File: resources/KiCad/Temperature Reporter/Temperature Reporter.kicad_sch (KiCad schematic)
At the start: 9 parts, among them U1 ESP32-C3-0.42-OLED, U2 DS18B20, U3 DS18B20

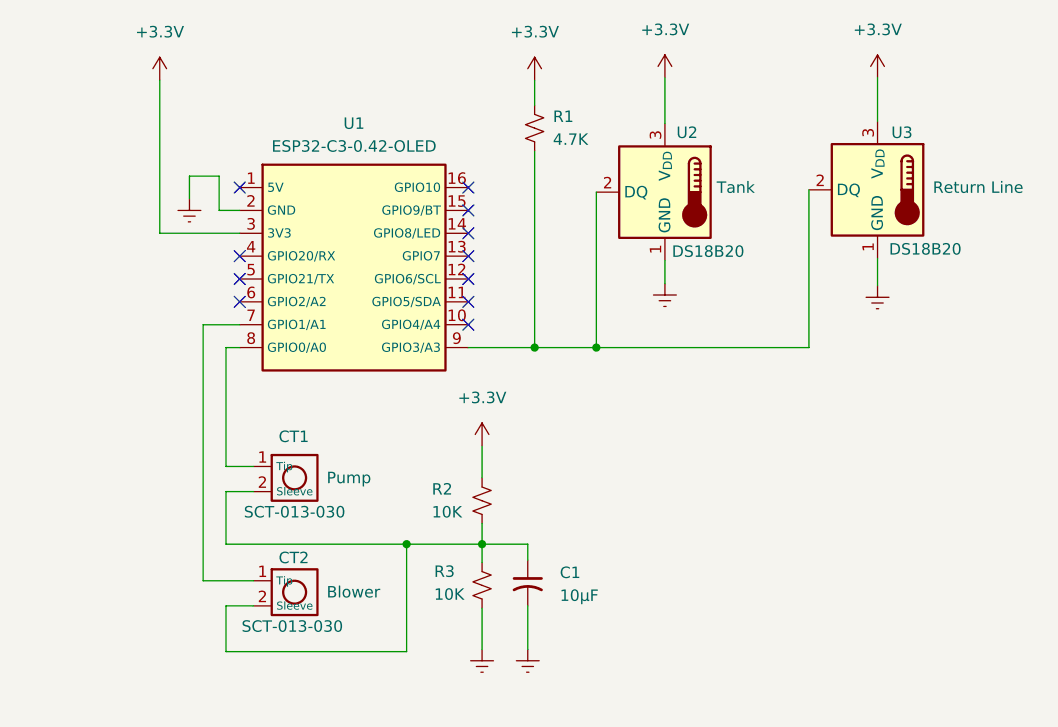
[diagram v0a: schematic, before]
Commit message: Added filter capacitors to the analog inputs
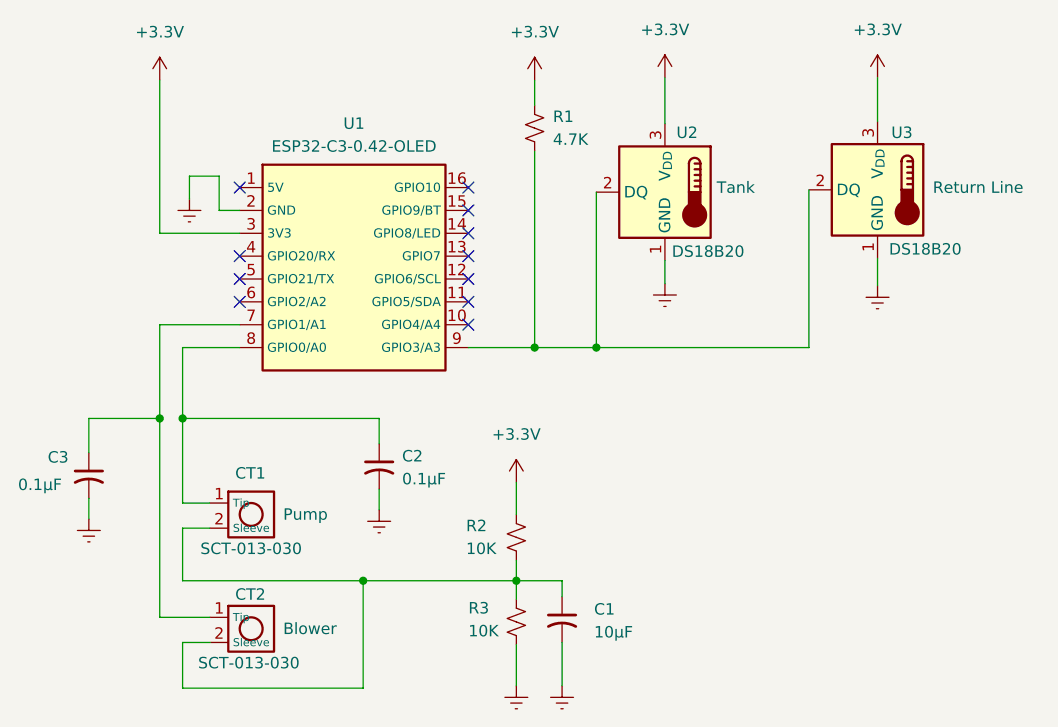
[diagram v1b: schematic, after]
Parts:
- added C2, C3: 0.1μF, symbol Device:C_Small_US
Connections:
- net Earth: now also C2.2, C3.2
- net at CT2.1 (Tip), U1.7 (GPIO1/A1): now also C3.1
- net at CT1.1 (Tip), U1.8 (GPIO0/A0): now also C2.1
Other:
- moved on the sheet: C1, CT1, CT2, R2, R3

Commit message: updated schematic
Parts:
- R2, R3: value 10K -> 1K
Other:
- moved on the sheet: C1, C2, C3, CT1, CT2, R2, R3, U1, U2, U3

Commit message: Changes to circuit board, board mount.  Added code to set the power to maximum.
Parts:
- C1, C2, C3: footprint (none) -> Capacitor_THT:C_Disc_D3.4mm_W2.1mm_P2.50mm
- CT1, CT2: footprint (none) -> Connector_PinHeader_2.54mm:PinHeader_1x02_P2.54mm_Horizontal
- R1, R2, R3: footprint (none) -> Resistor_THT:R_Axial_DIN0204_L3.6mm_D1.6mm_P2.54mm_Vertical
- U2, U3: footprint Package_TO_SOT_THT:TO-92_Inline -> Connector_PinHeader_2.54mm:PinHeader_1x03_P2.54mm_Horizontal
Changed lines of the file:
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@@
 			)
 		)
-		(property "Footprint" ""
+		(property "Footprint" "Capacitor_THT:C_Disc_D3.4mm_W2.1mm_P2.50mm"
 			(at 85.09 121.92 0)
 			(effects
@@
 			)
 		)
-		(property "Footprint" ""
+		(property "Footprint" "Connector_PinHeader_2.54mm:PinHeader_1x02_P2.54mm_Horizontal"
 			(at 103.632 138.43 0)
 			(effects
@@
 			)
 		)
-		(property "Footprint" "Package_TO_SOT_THT:TO-92_Inline"
+		(property "Footprint" "Connector_PinHeader_2.54mm:PinHeader_1x03_P2.54mm_Horizontal"
 			(at 198.12 96.52 0)
 			(effects
@@
 			)
 		)
-		(property "Footprint" ""
+		(property "Footprint" "Resistor_THT:R_Axial_DIN0204_L3.6mm_D1.6mm_P2.54mm_Vertical"
 			(at 132.08 128.27 0)
 			(effects
@@
 			)
 		)
-		(property "Footprint" ""
+		(property "Footprint" "Capacitor_THT:C_Disc_D3.4mm_W2.1mm_P2.50mm"
 			(at 137.16 137.16 0)
 			(effects
@@
 			)
 		)
-		(property "Footprint" "Package_TO_SOT_THT:TO-92_Inline"
+		(property "Footprint" "Connector_PinHeader_2.54mm:PinHeader_1x03_P2.54mm_Horizontal"
 			(at 173.99 96.52 0)
 			(effects
@@
 			)
 		)
-		(property "Footprint" ""
+		(property "Footprint" "Connector_PinHeader_2.54mm:PinHeader_1x02_P2.54mm_Horizontal"
 			(at 103.632 125.73 0)
 			(effects
@@
 			)
 		)
-		(property "Footprint" ""
+		(property "Footprint" "Capacitor_THT:C_Disc_D3.4mm_W2.1mm_P2.50mm"
 			(at 116.84 120.65 0)
 			(effects
@@
 			)
 		)
-		(property "Footprint" ""
+		(property "Footprint" "Resistor_THT:R_Axial_DIN0204_L3.6mm_D1.6mm_P2.54mm_Vertical"
 			(at 134.62 82.55 0)
 			(effects
@@
 			)
 		)
-		(property "Footprint" ""
+		(property "Footprint" "Resistor_THT:R_Axial_DIN0204_L3.6mm_D1.6mm_P2.54mm_Vertical"
 			(at 132.08 137.16 0)
 			(effects
